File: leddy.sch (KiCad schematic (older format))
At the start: 10 parts

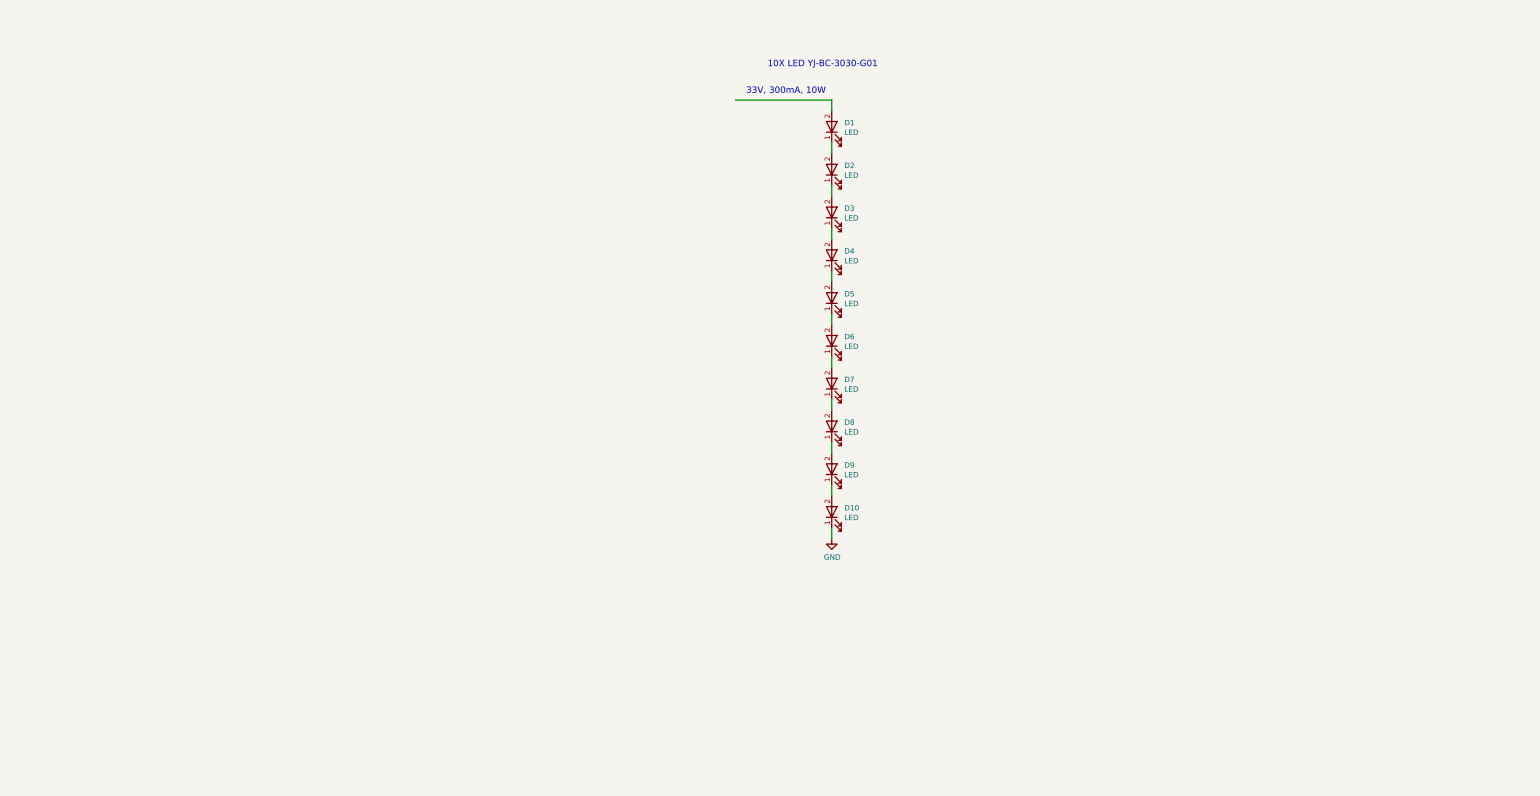
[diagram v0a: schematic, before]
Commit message: added LED driver IC and added a total of 50 LEDs
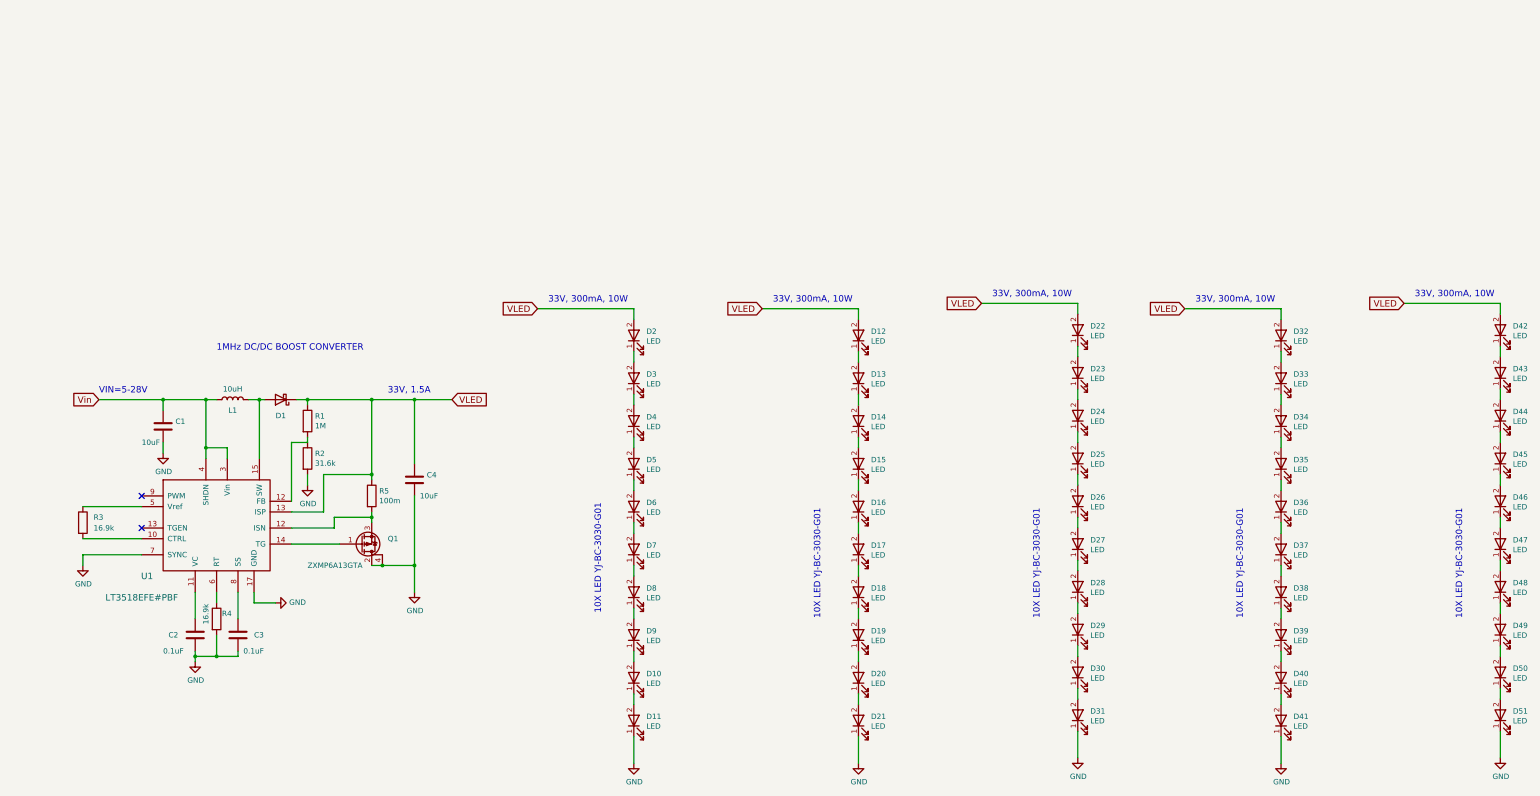
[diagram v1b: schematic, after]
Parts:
- added C1, C4: 10uF, Inductors_SMD:L_Vishay_IHLP-2020, symbol C
- added C2, C3: 0.1uF, Capacitors_SMD:C_0603_HandSoldering, symbol C
- added D1: SS3P4LHM3_A/H, TO_SOT_Packages_SMD:TO-277A, symbol D_Schottky
- added D12, D13, D14, D15, D16, D17, D18, D19, D20, D21, D22, D23, D24, D25, D26, D27, D28, D29, D30, D31, D32, D33, D34, D35, D36, D37, D38, D39, D40, D41, D42, D43, D44, D45, D46, D47, D48, D49, D50, D51: LED, lib:LED-3030, symbol LED
- added L1: 10uH, Inductors_SMD:L_Vishay_IHLP-2525, symbol L
- added Q1: ZXMP6A13GTA, TO_SOT_Packages_SMD:SOT-223, symbol Q_PMOS_GDSD
- added R1: 1M, Resistors_SMD:R_0603_HandSoldering, symbol R
- added R2: 31.6k, Resistors_SMD:R_0603_HandSoldering, symbol R
- added R3, R4: 16.9k, Resistors_SMD:R_0603_HandSoldering, symbol R
- added R5: 100m, Resistors_SMD:R_0603_HandSoldering, symbol R
- added U1: LT3518EFE#PBF, Housings_SSOP:TSSOP-16_4.4x5mm_Pitch0.65mm, symbol LT3518
- renumbered D9 to D10, D10 to D11, D1 to D2, D2 to D3, D3 to D4, D4 to D5, D5 to D6, D6 to D7, D7 to D8, D8 to D9
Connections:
- net labels added: VLED, Vin
- wire segments 12 -> 99
- no-connect marks 0 -> 2
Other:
- note added: "1MHz DC/DC BOOST CONVERTER"
- note added: "33V, 1.5A"
- note added: "VIN=5-28V"
- moved on the sheet: D10, D11, D2, D3, D4, D5, D6, D7, D8, D9

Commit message: layout almost done
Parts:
- added J1, J2, J3, J4: hole 1, Mounting_Holes:MountingHole_3.2mm_M3_ISO7380_Pad, symbol CONN_01X01
- added J5: umbrella support, Mounting_Holes:MountingHole_6.5mm, symbol CONN_01X01
- added R6, R8: 100m, Resistors_SMD:R_1206_HandSoldering, symbol R
- added R7, R9: 10k, Resistors_SMD:R_0603_HandSoldering, symbol R
- R2: value 31.6k -> 30.1k; Description RES 31.6k 1% 0603 -> RES 30.1k 1% 0603
- R3, R4: value 16.9k -> 16.2k; Description RES 16.9k 1% 0603 -> RES 16.2k 1% 0603
- R5: value 100m -> 10k; Description RES 100m 1% 0603 -> RES 10k 1% 0603
- U1: footprint Housings_SSOP:TSSOP-16_4.4x5mm_Pitch0.65mm -> Housings_SSOP:TSSOP-16-1EP_4.4x5mm_Pitch0.65mm; Description (none) -> Full-Featured LED Driver with 2.3A Switch Current; MAN (none) -> Linear Technology; SUP Linear Technology -> (none)
- renumbered D2 to D1, D11 to D10, D1 to D100, D12 to D11, D13 to D12, D14 to D13, D15 to D14, D16 to D15, D17 to D16, D18 to D17, D19 to D18, D20 to D19, D3 to D2, D21 to D20, D22 to D21, D23 to D22, D24 to D23, D25 to D24, D26 to D25, D27 to D26, D28 to D27, D29 to D28, D30 to D29, D4 to D3, D31 to D30, D32 to D31, D33 to D32, D34 to D33, D35 to D34, D36 to D35, D37 to D36, D38 to D37, D39 to D38, D40 to D39, D5 to D4, D41 to D40, D42 to D41, D43 to D42, D44 to D43, D45 to D44, D46 to D45, D47 to D46, D48 to D47, D49 to D48, D50 to D49, D6 to D5, D51 to D50, D7 to D6, D8 to D7, D9 to D8, D10 to D9
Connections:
- net GND: now also R5.2, R7.2, R9.2
- net VLED: now also R6.1, R8.1; no longer R5.1
- net CTRL: now reaches R3.2, U1.10 (CTRL)
- net CTRL: now also R5.1, R7.1, R9.1
- new net: Q1.3 (S), R6.2, R8.2, U1.12 (ISN)
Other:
- note added: "33V, 2A"
- note added: "SET MAX Iout"
- note removed: "33V, 1.5A"
- moved on the sheet: C1, C2, C3, C4, D1, D10, D100, D11, D12, D13, D14, D15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
